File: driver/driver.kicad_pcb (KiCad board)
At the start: 2 copper layers, 31 x 27 mm, 3 parts, among them J101 UJC-HP-3-SMT-TR

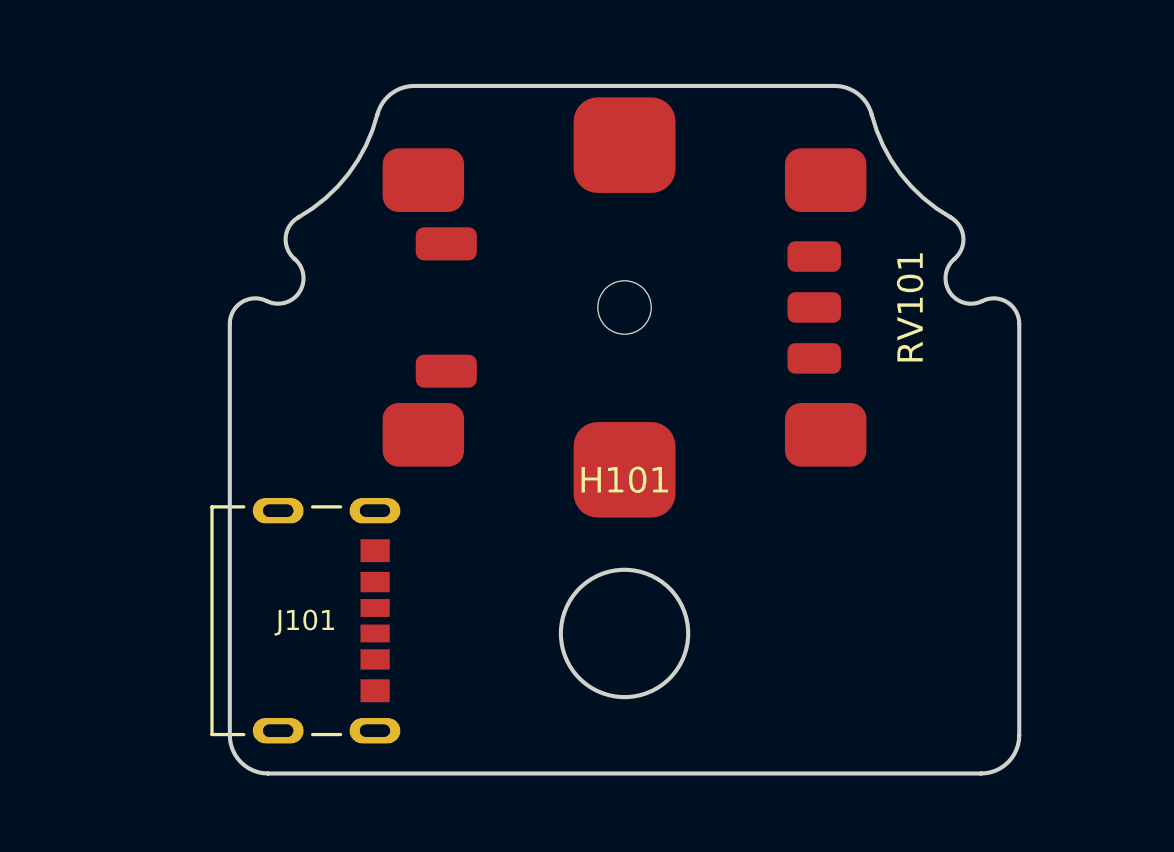
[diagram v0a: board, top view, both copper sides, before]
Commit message: Start placing connectors
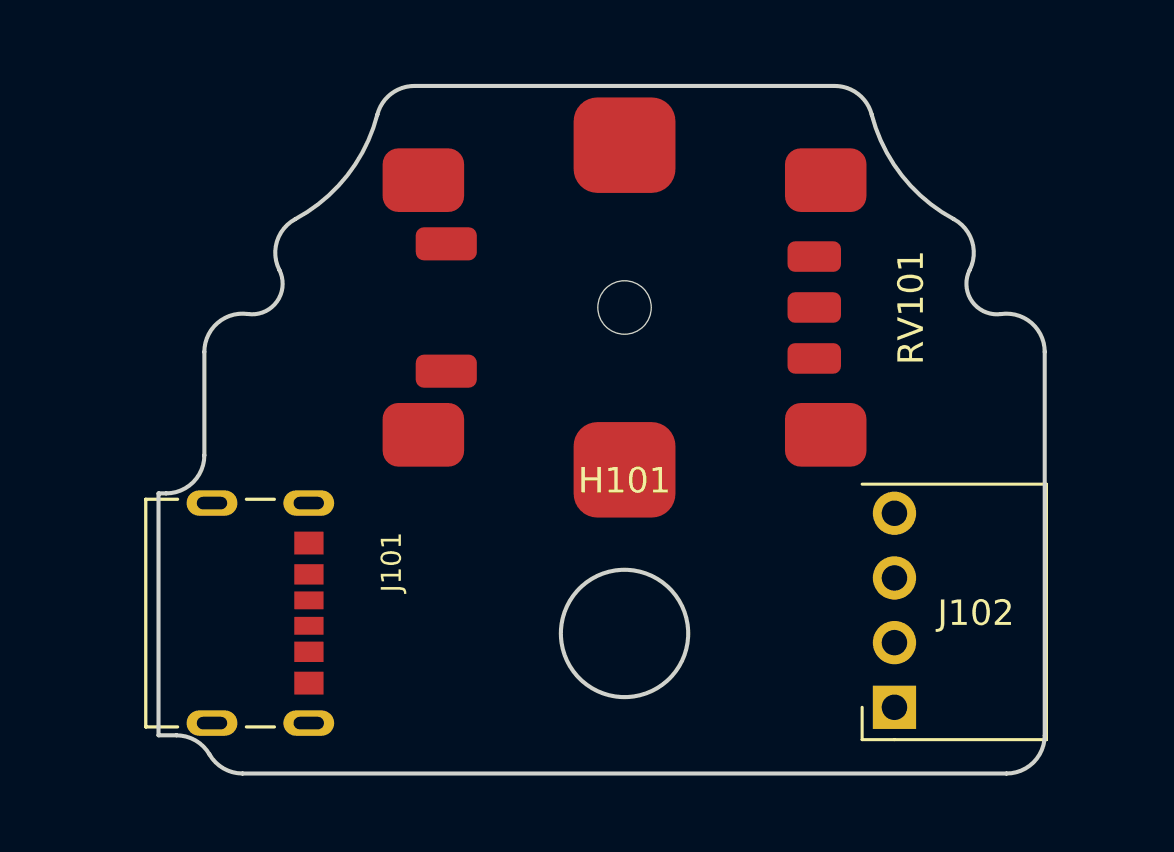
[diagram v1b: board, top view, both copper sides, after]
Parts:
- added J102: fan_header_4pin, proj:fan_header_4pin_right_angle, F.Cu at (90.6, 78.9)
- moved J101 2.62 mm to (67.6, 75.2)
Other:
- board size 31 x 27 mm -> 34.8 x 27 mm

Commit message: First PCB routing
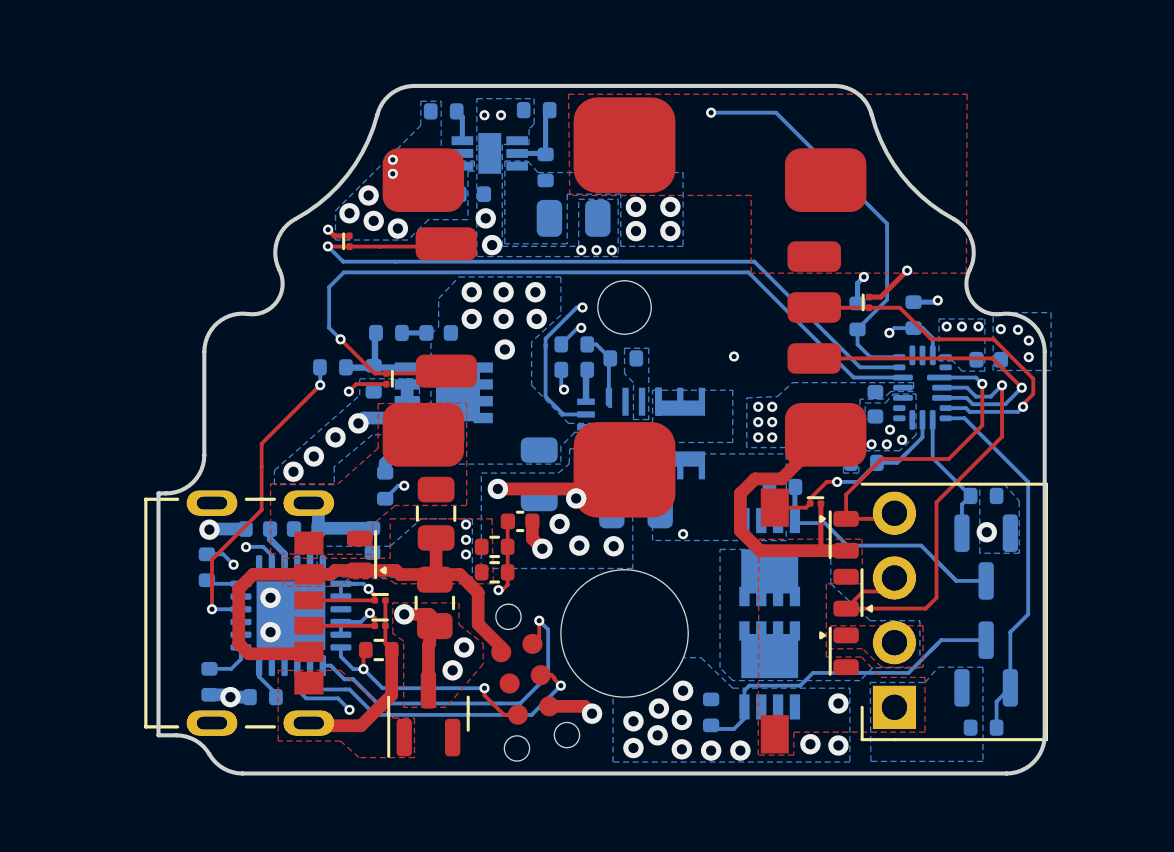
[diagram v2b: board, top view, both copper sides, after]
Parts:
- added C101: 10u, proj:C_0805_2012Metric, B.Cu at (76.7, 69.8)
- added C102: 4.7u, proj:C_0805_2012Metric, F.Cu at (72.6, 71.3)
- added C103: 1u, proj:C_0402_1005Metric, F.Cu at (75.9, 71.6)
- added C104: 22u, proj:C_0805_2012Metric, B.Cu at (80.5, 71.2)
- added C105: 1u, proj:C_0402_1005Metric, B.Cu at (70.1, 72.3)
- added C106: 1u, proj:C_0402_1005Metric, B.Cu at (65.6, 71.9)
- added C107: 1u, proj:C_0402_1005Metric, B.Cu at (67.5, 71.9)
- added C108: 100n, proj:C_0402_1005Metric, B.Cu at (72.7, 64.2)
- added C109: 1u, proj:C_0402_1005Metric, B.Cu at (74.0, 58.8)
- added C110: 4u7, proj:C_0805_2012Metric, B.Cu at (78.0, 59.7)
- added C111: 1u, proj:C_0402_1005Metric, B.Cu at (94.3, 65.2)
- added C112: 1u, proj:C_0402_1005Metric, B.Cu at (89.8, 67.0)
- added D101: uclamp2271p, proj:uClampxx71P, F.Cu at (69.6, 72.9)
- added D102: uclamp2411za, proj:uClamp2411ZA, F.Cu at (70.4, 75.7)
- added D103: uclamp2411za, proj:uClamp2411ZA, F.Cu at (70.4, 74.7)
- added D104: D_Schottky, proj:Schottky_0402, F.Cu at (74.9, 72.6)
- added D105: uclamp2271p, proj:uClampxx71P, F.Cu at (88.7, 76.7)
- added D106: uclamp2271p, proj:uClampxx71P, F.Cu at (88.7, 74.4)
- added D107: uclamp2271p, proj:uClampxx71P, F.Cu at (88.7, 72.1)
- added D108: uclamp2411za, proj:uClamp2411ZA, F.Cu at (69.2, 60.6)
- added D109: uclamp2411za, proj:uClamp2411ZA, F.Cu at (70.7, 66.0)
- added D110: uclamp2411za, proj:uClamp2411ZA, F.Cu at (89.6, 63.0)
- added D111: 14V, proj:SOT-23, F.Cu at (72.3, 79.2)
- added D112: uclamp2411za, proj:uClamp2411ZA, F.Cu at (87.5, 70.9)
- added F101: 1A, proj:R_0805_2012Metric, F.Cu at (72.5, 74.8)
- added J103: TagConnect-2x3, proj:Tag-Connect_TC2030-IDC-NL_2x03_P1.27mm_Vertical, F.Cu at (76.1, 77.8)
- added Q101: SiSS63DN, proj:Vishay_PowerPAK_1212-8_Single, B.Cu at (85.7, 73.0)
- added Q102: SiSS63DN, proj:Vishay_PowerPAK_1212-8_Single, B.Cu at (85.7, 77.5)
- added Q103: FDV301N, proj:SOT-23, B.Cu at (94.2, 73.0)
- added Q104: FDV301N, proj:SOT-23, B.Cu at (94.2, 77.2)
- added Q105: SiSS63DN, proj:Vishay_PowerPAK_1212-8_Single, B.Cu at (72.9, 66.5)
- added R101: 100k, proj:R_0402_1005Metric, B.Cu at (91.3, 63.5)
- added R102: 45k3, proj:R_0402_1005Metric, B.Cu at (78.0, 65.7)
- added R103: 470, proj:R_0402_1005Metric, F.Cu at (74.9, 73.6)
- added R104: 1k, proj:R_0402_1005Metric, B.Cu at (63.6, 73.4)
- added R105: 100k, proj:R_0402_1005Metric, B.Cu at (78.0, 64.7)
- added R106: 19k1, proj:R_0402_1005Metric, B.Cu at (80.0, 65.2)
- added R107: 100k, proj:R_0402_1005Metric, F.Cu at (70.3, 76.7)
- added R108: 100k, proj:R_0402_1005Metric, B.Cu at (65.8, 78.5)
- added R109: 100k, proj:R_0402_1005Metric, B.Cu at (63.7, 77.9)
- added R110: 100k, proj:R_0402_1005Metric, B.Cu at (86.2, 70.2)
- added R111: 100k, proj:R_0402_1005Metric, B.Cu at (83.4, 79.1)
- added R112: 100k, proj:R_0402_1005Metric, B.Cu at (94.1, 70.6)
- added R113: 100k, proj:R_0402_1005Metric, B.Cu at (94.1, 79.7)
- added R114: 22k, proj:R_0402_1005Metric, B.Cu at (68.5, 65.5)
- added R115: 1k, proj:R_0402_1005Metric, B.Cu at (70.6, 70.2)
- added R116: 100k, proj:R_0402_1005Metric, B.Cu at (70.2, 66.0)
- added R117: 100, proj:R_0402_1005Metric, B.Cu at (70.8, 64.2)
- added R118: 100k, proj:R_0402_1005Metric, B.Cu at (72.9, 55.5)
- added R119: 18k, proj:R_0402_1005Metric, B.Cu at (76.9, 57.7)
- added R120: 10k, proj:R_0402_1005Metric, B.Cu at (76.5, 55.5)
- added R121: 100k, proj:R_0402_1005Metric, B.Cu at (89.4, 69.3)
- added R122: 100k, proj:R_0402_1005Metric, B.Cu at (89.2, 63.5)
- added SW101: A6S-1101-H, proj:A6S-1101-H, F.Cu at (85.9, 75.5)
- added U101: STUSB4500QTR, Package_DFN_QFN:QFN-24-1EP_4x4mm_P0.5mm_EP2.7x2.7mm, B.Cu at (66.9, 75.3)
- added U102: MPM3606, proj:MPM3606, B.Cu at (80.9, 68.2)
- added U103: SLG46621, proj:SLG46621V, B.Cu at (91.7, 66.3)
- added U104: LDL212PVR, proj:LDL212PVR, B.Cu at (74.7, 57.1)
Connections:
- net Net-(J101-PadA9) renamed V_{bus}
- J101 pad A12: Net-(J101-PadA12) -> GND
- J101 pad A5: unconnected-(J101-PadA5) -> /CC1
- J101 pad B12: Net-(J101-PadA12) -> GND
- J101 pad B5: unconnected-(J101-PadB5) -> /CC2
- J101 pad S1: Net-(J101-PadS1) -> GND
- J101 pad S2: Net-(J101-PadS1) -> GND
- J101 pad S3: Net-(J101-PadS1) -> GND
- J101 pad S4: Net-(J101-PadS1) -> GND
- J102 pad 1: unconnected-(J102-Pad1) -> GND
- J102 pad 2: unconnected-(J102-Pad2) -> /FAN_PWR
- J102 pad 3: unconnected-(J102-Pad3) -> /FAN_TACHO
- J102 pad 4: unconnected-(J102-Pad4) -> /FAN_PWM
- RV101 pad 1: unconnected-(RV101-Pad1) -> /POT_SUPPLY
- RV101 pad 2: unconnected-(RV101-Pad2) -> /POT_WIPER
- RV101 pad 3: unconnected-(RV101-Pad3) -> GND
- RV101 pad 4: unconnected-(RV101-Pad4) -> /SW2
- RV101 pad 5: unconnected-(RV101-Pad5) -> /SW1
- RV101 pad MP: unconnected-(RV101-PadMP) -> GND
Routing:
- net /HI_PWR: track 0.00 -> 49.6 mm, vias 0 -> 2
- net GND: track 0.00 -> 45.7 mm, vias 0 -> 34
- net /SW2: track 0.00 -> 31.5 mm, vias 0 -> 1
- net /SW1: track 0.00 -> 29.1 mm, vias 0 -> 1
- net /REG_EN: track 0.00 -> 24.2 mm, vias 0 -> 3
- net Net-(C103-Pad1): track 0.00 -> 21.8 mm, vias 0 -> 2
- net V_{bus}: track 0.00 -> 20.0 mm, vias 0 -> 3
- net /FAN_TACHO: track 0.00 -> 18.2 mm, vias 0 -> 1
- net Net-(R115-Pad1): track 0.00 -> 16.4 mm, vias 0 -> 2
- net Net-(D111-Pad3): track 0.00 -> 16.2 mm, vias 0 -> 7
- net /FAN_V_{snk}: track 0.00 -> 14.4 mm
- net /POT_WIPER: track 0.00 -> 14.2 mm, vias 0 -> 1
- net Net-(Q102-Pad4): track 0.00 -> 13.4 mm
- net /PROG_SCL: track 0.00 -> 13.2 mm, vias 0 -> 1
- net /FAN_PWM: track 0.00 -> 12.8 mm, vias 0 -> 1
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- added copper zone on B.Cu, net +3.3V
- added copper zone on In1.Cu, net +3.3V
- added copper zone on B.Cu, net +5V
- added copper zone on B.Cu, net /AGND
- added copper zone on B.Cu, net /FAN_PWR
- added copper zone on F.Cu, net /FAN_PWR
- added copper zone on B.Cu, net GND
- added copper zone on F.Cu, net GND
- added copper zone on In2.Cu, net GND
- added copper zone on B.Cu, net Net-(D111-Pad3)
- added copper zone on F.Cu, net Net-(D111-Pad3)
- added copper zone on In1.Cu, net Net-(D111-Pad3)
- added copper zone on B.Cu, net V_{bus}
- added copper zone on F.Cu, net V_{bus}
- added copper zone on B.Cu, net V_{snk}
- added copper zone on In1.Cu, net V_{snk}
- added copper zone on B.Cu, net unconnected-(U102-Pad11)
- added copper zone on B.Cu, net unconnected-(U102-Pad4,5,6)
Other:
- outline, holes or cut-outs redrawn
- copper layers 2 -> 4

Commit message: Change the 5V power switch mosfet to a controller with reverse voltage protection
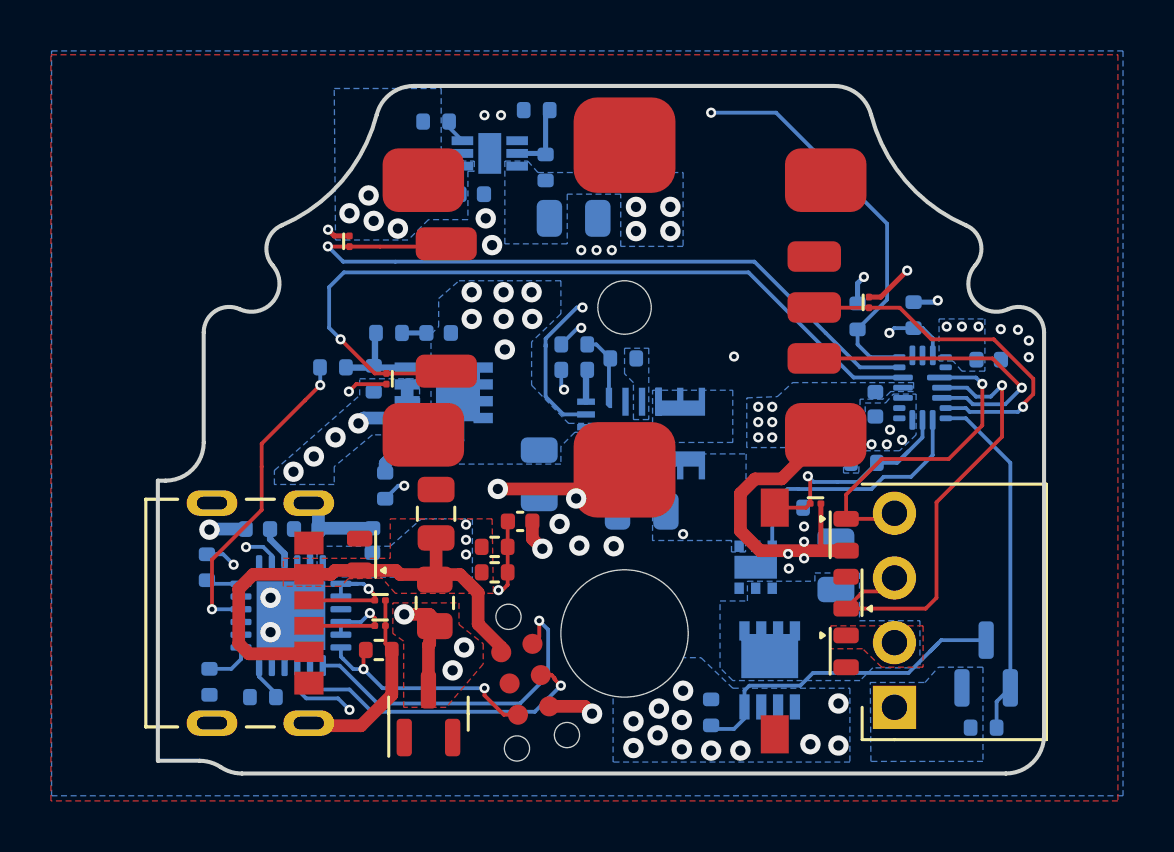
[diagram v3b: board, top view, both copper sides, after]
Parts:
- removed Q101: SiSS63DN, proj:Vishay_PowerPAK_1212-8_Single
- removed Q103: FDV301N, proj:SOT-23
- removed R110: 100k, proj:R_0402_1005Metric
- added C113: 22u, proj:C_0805_2012Metric, B.Cu at (88.3, 73.3)
- added U105: AP22814ASN-7, proj:Diodes_UDFN2020-6, B.Cu at (85.2, 73.4)
- moved R112 7.61 mm to (86.5, 71.1)
- moved R118 0.50 mm to (72.6, 55.9)
- moved C104 0.23 mm to (80.7, 71.2)
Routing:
- net Net-(Q101-Pad4): track 11.0 -> 0.00 mm
- net /FAN_5V: track 5.21 -> 10.1 mm
- net GND: track 45.7 -> 44.0 mm, vias 34 -> 35
- net /FAN_VOLTAGE_SEL: track 8.38 -> 9.21 mm
- net /FAN_V_{snk}: track 14.4 -> 13.9 mm
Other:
- outline, holes or cut-outs redrawn
